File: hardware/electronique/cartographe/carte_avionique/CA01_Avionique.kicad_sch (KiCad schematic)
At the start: 0 parts

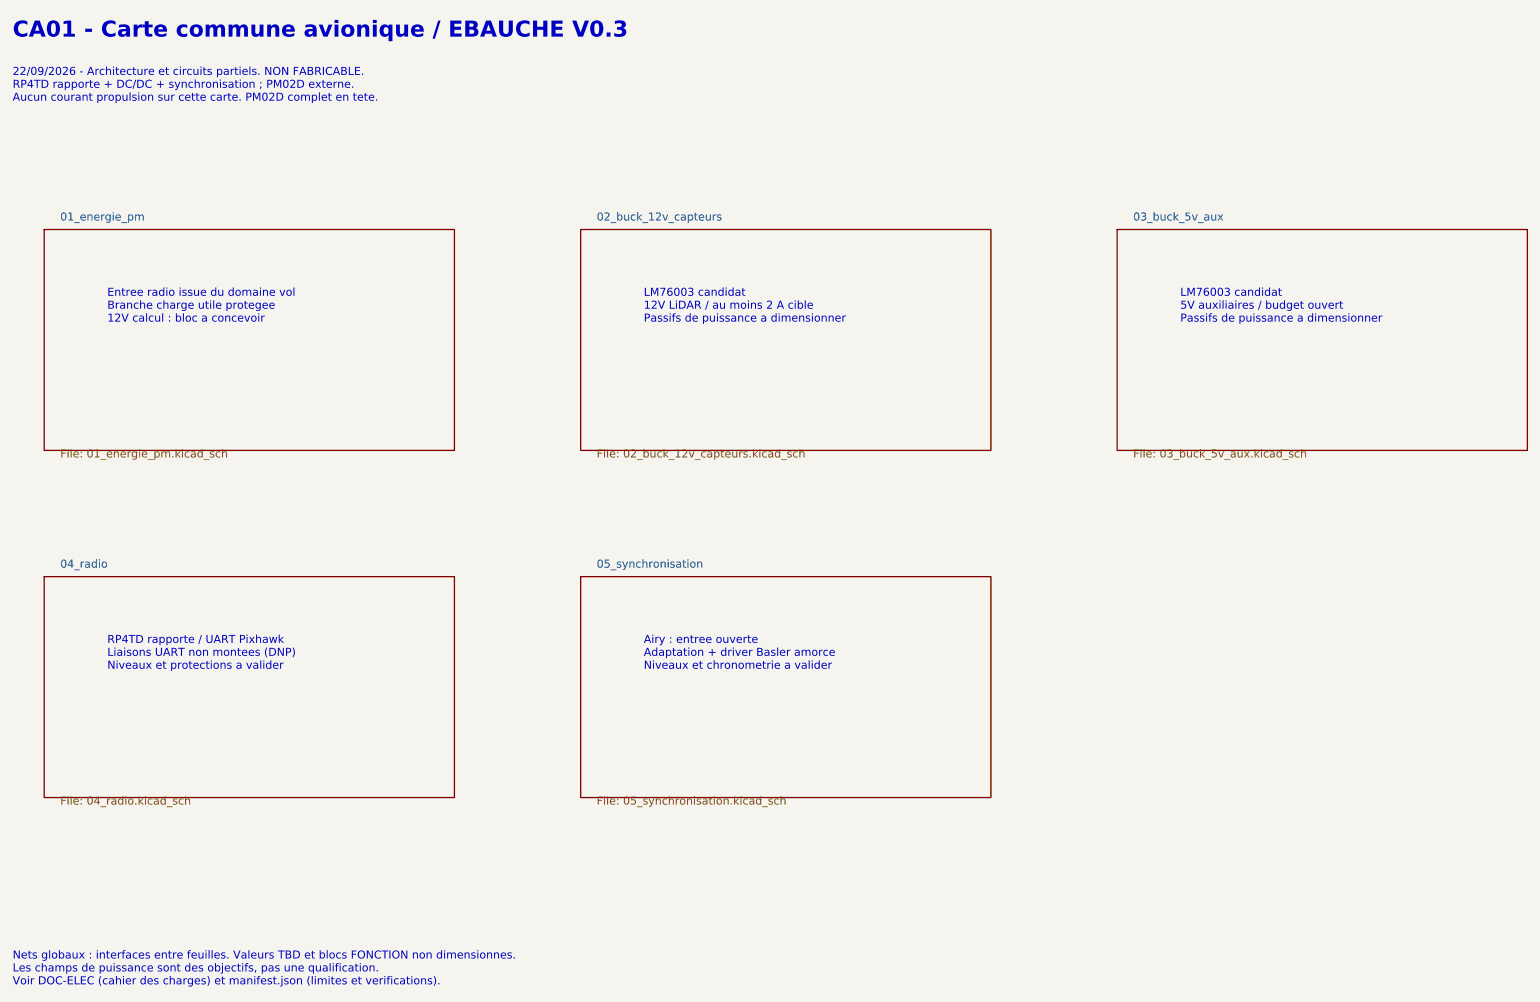
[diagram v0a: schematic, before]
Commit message: feat(hw): compléter CA01 et clarifier la synchronisation des captures
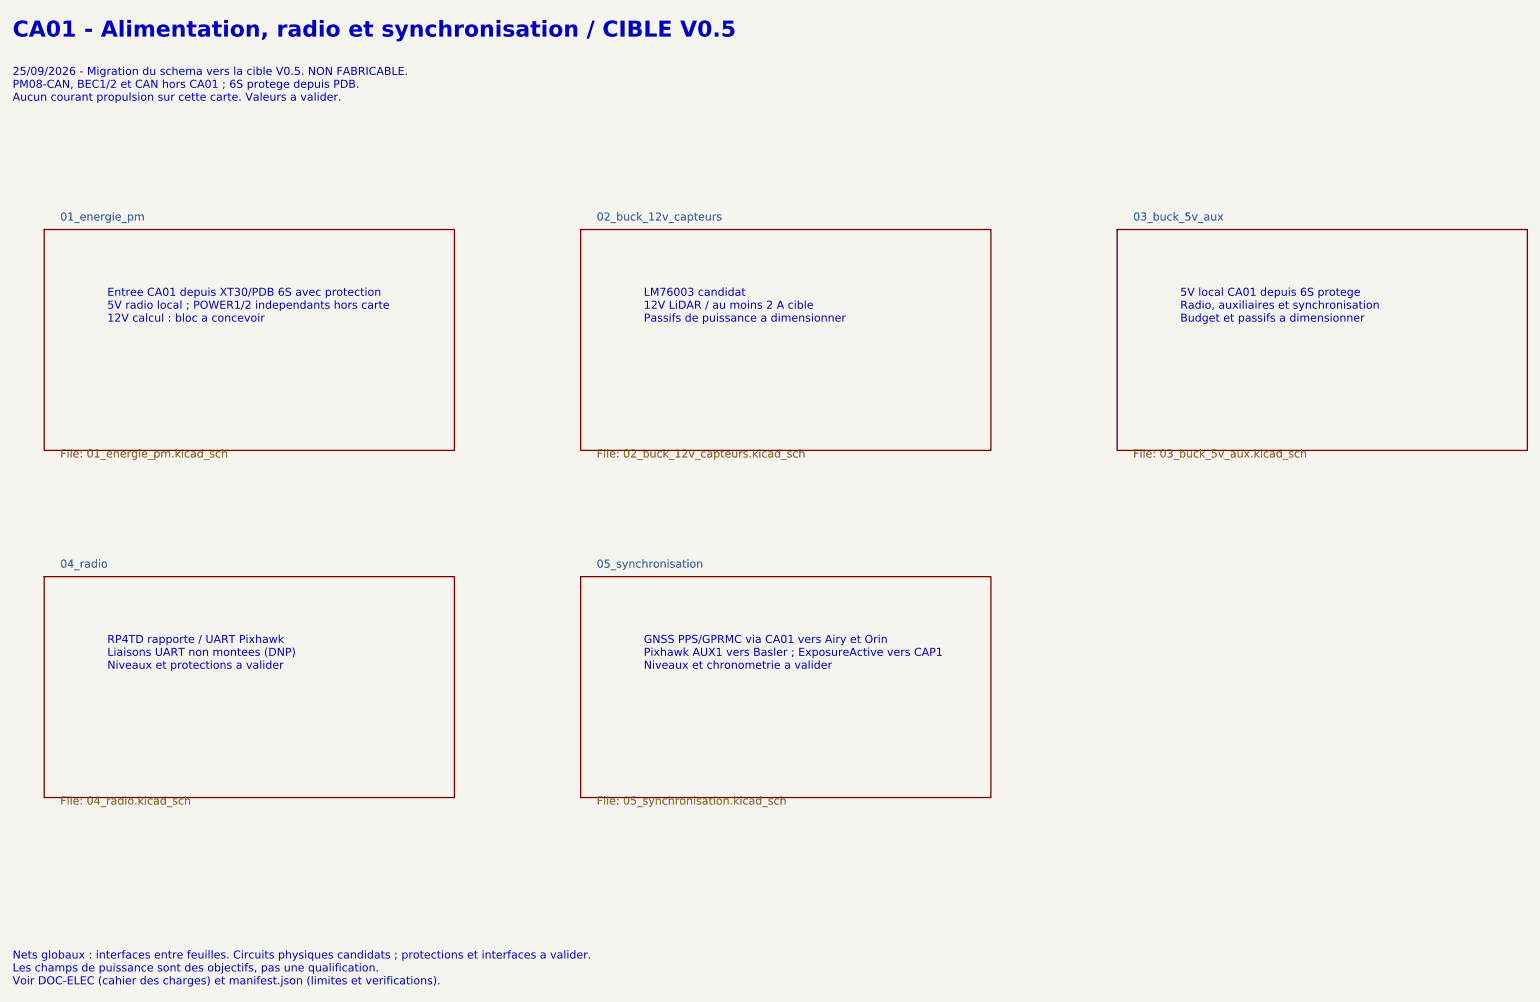
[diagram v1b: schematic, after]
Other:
- note added: "25/09/2026 - Migration du schema vers la cible V0.5. NON FABRICABLE. PM08-CAN, BEC1/2 et CAN hors CA01 ; 6S protege depuis PDB. Aucun courant propulsion sur cette carte. Valeurs a valider."
- note added: "5V local CA01 depuis 6S protege Radio, auxiliaires et synchronisation Budget et passifs a dimensionner"
- note added: "CA01 - Alimentation, radio et synchronisation / CIBLE V0.5"
- note added: "Entree CA01 depuis XT30/PDB 6S avec protection 5V radio local ; POWER1/2 independants hors carte 12V calcul : bloc a concevoir"
- note added: "GNSS PPS/GPRMC via CA01 vers Airy et Orin Pixhawk AUX1 vers Basler ; ExposureActive vers CAP1 Niveaux et chronometrie a valider"
- note added: "Nets globaux : interfaces entre feuilles. Circuits physiques candidats ; protections et interfaces a valider. Les champs de puissance sont des objectifs, pas une qualification. Voir DOC-ELEC (cahier des charges) et manifest.json (limites et verifications)."
- note removed: "22/09/2026 - Architecture et circuits partiels. NON FABRICABLE. RP4TD rapporte + DC/DC + synchronisation ; PM02D externe. Aucun courant propulsion sur cette carte. PM02D complet en tete."
- note removed: "Airy : entree ouverte Adaptation + driver Basler amorce Niveaux et chronometrie a valider"
- note removed: "CA01 - Carte commune avionique / EBAUCHE V0.3"
- note removed: "Entree radio issue du domaine vol Branche charge utile protegee 12V calcul : bloc a concevoir"
- note removed: "LM76003 candidat 5V auxiliaires / budget ouvert Passifs de puissance a dimensionner"
- note removed: "Nets globaux : interfaces entre feuilles. Valeurs TBD et blocs FONCTION non dimensionnes. Les champs de puissance sont des objectifs, pas une qualification. Voir DOC-ELEC (cahier des charges) et manifest.json (limites et verifications)."
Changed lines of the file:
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@@
 	(generator_version "10.0")
 	(paper "A4")
-	(text "LM76003 candidat\n5V auxiliaires / budget ouvert\nPassifs de puissance a dimensionner"
+	(text "5V local CA01 depuis 6S protege\nRadio, auxiliaires et synchronisation\nBudget et passifs a dimensionner"
 		(exclude_from_sim no)
 		(at 205 65 0)
@@
 		)
 	)
-	(text "CA01 - Carte commune avionique / EBAUCHE V0.3"
+	(text "CA01 - Alimentation, radio et synchronisation / CIBLE V0.5"
 		(exclude_from_sim no)
 		(at 20 20 0)
@@
 		)
 	)
-	(text "22/09/2026 - Architecture et circuits partiels. NON FABRICABLE.\nRP4TD rapporte + DC/DC + synchronisation ; PM02D externe.\nAucun courant propulsion sur cette carte. PM02D complet en tete."
+	(text "25/09/2026 - Migration du schema vers la cible V0.5. NON FABRICABLE.\nPM08-CAN, BEC1/2 et CAN hors CA01 ; 6S protege depuis PDB.\nAucun courant propulsion sur cette carte. Valeurs a valider."
 		(exclude_from_sim no)
 		(at 20 30 0)
@@
 		)
 	)
-	(text "Entree radio issue du domaine vol\nBranche charge utile protegee\n12V calcul : bloc a concevoir"
+	(text "Entree CA01 depuis XT30/PDB 6S avec protection\n5V radio local ; POWER1/2 independants hors carte\n12V calcul : bloc a concevoir"
 		(exclude_from_sim no)
 		(at 35 65 0)
@@
 		)
 	)
-	(text "Nets globaux : interfaces entre feuilles. Valeurs TBD et blocs FONCTION non dimensionnes.\nLes champs de puissance sont des objectifs, pas une qualification.\nVoir DOC-ELEC (cahier des charges) et manifest.json (limites et verifications)."
+	(text "Nets globaux : interfaces entre feuilles. Circuits physiques candidats ; protections et interfaces a valider.\nLes champs de puissance sont des objectifs, pas une qualification.\nVoir DOC-ELEC (cahier des charges) et manifest.json (limites et verifications)."
 		(exclude_from_sim no)
 		(at 20 170 0)
@@
 		)
 	)
-	(text "Airy : entree ouverte\nAdaptation + driver Basler amorce\nNiveaux et chronometrie a valider"
+	(text "GNSS PPS/GPRMC via CA01 vers Airy et Orin\nPixhawk AUX1 vers Basler ; ExposureActive vers CAP1\nNiveaux et chronometrie a valider"
 		(exclude_from_sim no)
 		(at 120 120 0)
